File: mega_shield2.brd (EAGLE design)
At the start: 103.8 x 58.7 mm, 36 parts, among them IC1 L298, IC2 LM2937ET-5V, J2 Mega R3

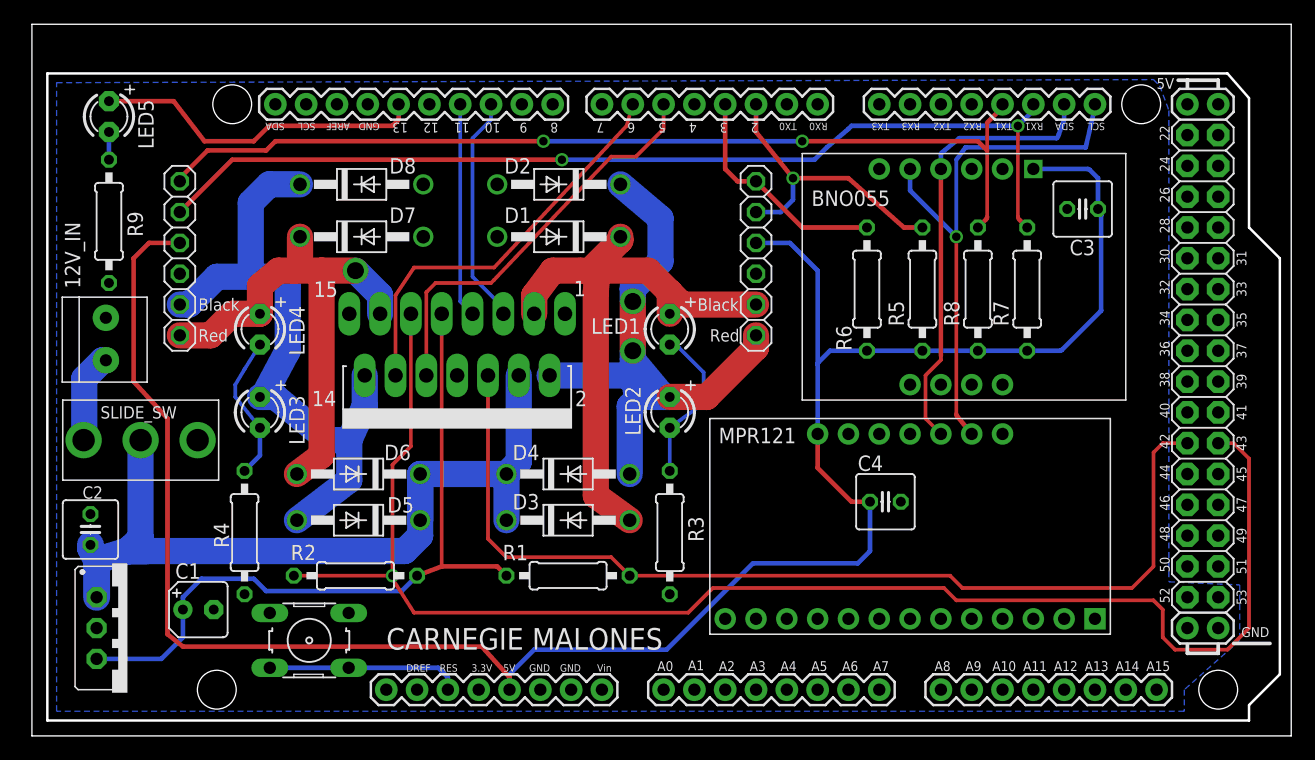
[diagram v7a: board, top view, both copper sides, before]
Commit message: shifted some components around, edited silkscreen
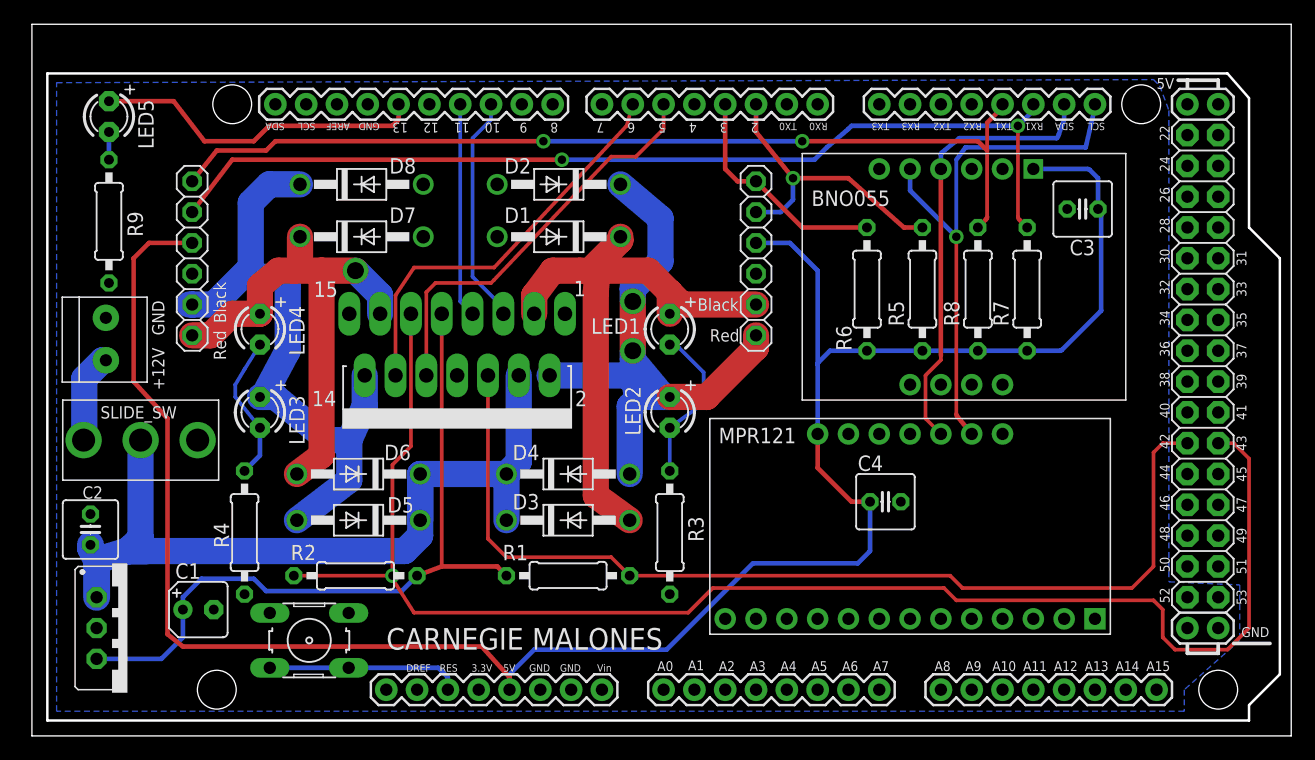
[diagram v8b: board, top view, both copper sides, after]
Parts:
- moved JP2 1.02 mm to (13.2, 39.4)
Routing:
- net MEGA18: track 79.7 -> 78.4 mm
- net MOT3: track 43.1 -> 42.1 mm
- net MEGA_5V: track 176.6 -> 177.6 mm
- net MEGA19: track 83.0 -> 82.3 mm
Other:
- board text added: "+12V"
- board text added: "GND"
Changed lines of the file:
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@@
 <text x="29.21" y="7.112" size="1.778" layer="25">CARNEGIE MALONES</text>
 <polygon width="0.3048" layer="42">
-<vertex x="58.42" y="32.512"/>
+<vertex x="58.674" y="32.004"/>
 <vertex x="58.42" y="32.004"/>
 <vertex x="56.134" y="29.718"/>
 <vertex x="56.134" y="27.432"/>
 <vertex x="56.388" y="27.178"/>
-<vertex x="60.452" y="31.242"/>
-<vertex x="59.69" y="31.242"/>
+<vertex x="59.944" y="30.734"/>
 </polygon>
 <polygon width="0.3048" layer="42">
@@
 <vertex x="33.528" y="16.002"/>
 <vertex x="32.004" y="14.478"/>
-<vertex x="32.004" y="14.224"/>
-<vertex x="32.766" y="13.462"/>
+<vertex x="33.02" y="13.462"/>
 <vertex x="35.306" y="13.462"/>
 <vertex x="38.354" y="16.51"/>
@@
 <vertex x="37.592" y="19.812"/>
 <vertex x="37.338" y="20.066"/>
-</polygon>
-<polygon width="0.4064" layer="42">
-<vertex x="13.716" y="34.29"/>
-<vertex x="13.208" y="34.29"/>
-<vertex x="13.97" y="33.274"/>
-<vertex x="13.97" y="32.512"/>
-<vertex x="13.462" y="32.004"/>
-<vertex x="15.24" y="32.004"/>
-<vertex x="16.764" y="33.528"/>
-<vertex x="16.764" y="33.782"/>
-<vertex x="16.256" y="34.29"/>
-<vertex x="16.256" y="36.322"/>
-<vertex x="15.748" y="36.322"/>
 </polygon>
 <polygon width="0.4064" layer="42">
@@
 <vertex x="72.898" y="32.766"/>
 <vertex x="72.39" y="32.258"/>
-<vertex x="69.596" y="32.258"/>
-<vertex x="69.088" y="32.766"/>
+<vertex x="70.104" y="32.258"/>
+<vertex x="69.342" y="32.766"/>
 <vertex x="68.326" y="32.766"/>
 <vertex x="67.818" y="32.258"/>
@@
 <wire x1="18.542" y1="53.848" x2="18.542" y2="50.8" width="0.4064" layer="42"/>
 <wire x1="18.542" y1="50.8" x2="17.272" y2="48.514" width="0.4064" layer="42"/>
-<wire x1="17.272" y1="48.514" x2="14.478" y2="43.434" width="0.4064" layer="42"/>
-<wire x1="14.478" y1="43.434" x2="13.716" y2="41.91" width="0.4064" layer="42"/>
+<wire x1="17.272" y1="48.514" x2="14.224" y2="42.164" width="0.4064" layer="42"/>
 <wire x1="13.716" y1="41.91" x2="7.874" y2="41.91" width="0.4064" layer="42"/>
 <wire x1="7.874" y1="41.91" x2="2.54" y2="36.576" width="0.4064" layer="42"/>
@@
 <vertex x="15.24" y="31.496"/>
 </polygon>
-<text x="13.716" y="32.512" size="1.016" layer="25">Red</text>
+<text x="16.002" y="30.988" size="1.016" layer="25" rot="R90">Red</text>
 <text x="55.88" y="32.512" size="1.016" layer="25">Red</text>
 <text x="54.864" y="35.052" size="1.016" layer="25">Black</text>
-<text x="13.716" y="35.052" size="1.016" layer="25">Black</text>
+<text x="16.002" y="34.036" size="1.016" layer="25" rot="R90">Black</text>
+<text x="10.922" y="33.02" size="1.016" layer="25" rot="R90">GND</text>
+<text x="9.906" y="32.004" size="1.016" layer="25" rot="R270">+12V</text>
 </plain>
 <attributes>
@@
 </class>
 </classes>
-<designrules name="default">
-<description language="de">&lt;b&gt;EAGLE Design Rules&lt;/b&gt;
-&lt;p&gt;
-Die Standard-Design-Rules sind so gewählt, dass sie für
-die meisten Anwendungen passen. Sollte ihre Platine
-besondere Anforderungen haben, treffen Sie die erforderlichen
-Einstellungen hier und speichern die Design Rules unter
-einem neuen Namen ab.</description>
+<designrules name="SparkFun">
 <description language="en">&lt;b&gt;EAGLE Design Rules&lt;/b&gt;
 &lt;p&gt;
@@
 <param name="mdViaViaSameLayer" value="8mil"/>
 <param name="mnLayersViaInSmd" value="2"/>
-<param name="mdCopperDimension" value="40mil"/>
+<param name="mdCopperDimension" value="10mil"/>
 <param name="mdDrill" value="8mil"/>
 <param name="mdSmdStop" value="0mil"/>
-<param name="msWidth" value="10mil"/>
-<param name="msDrill" value="24mil"/>
+<param name="msWidth" value="8mil"/>
+<param name="msDrill" value="20mil"/>
 <param name="msMicroVia" value="9.99mm"/>
 <param name="msBlindViaRatio" value="0.5"/>
@@
 <param name="rvMicroViaOuter" value="0.25"/>
 <param name="rvMicroViaInner" value="0.25"/>
-<param name="rlMinPadTop" value="10mil"/>
+<param name="rlMinPadTop" value="12mil"/>
 <param name="rlMaxPadTop" value="20mil"/>
 <param name="rlMinPadInner" value="10mil"/>
 <param name="rlMaxPadInner" value="20mil"/>
-<param name="rlMinPadBottom" value="10mil"/>
+<param name="rlMinPadBottom" value="12mil"/>
 <param name="rlMaxPadBottom" value="20mil"/>
-<param name="rlMinViaOuter" value="8mil"/>
+<param name="rlMinViaOuter" value="10mil"/>
 <param name="rlMaxViaOuter" value="20mil"/>
-<param name="rlMinViaInner" value="8mil"/>
+<param name="rlMinViaInner" value="10mil"/>
 <param name="rlMaxViaInner" value="20mil"/>
 <param name="rlMinMicroViaOuter" value="4mil"/>
@@
 <param name="mlMinCreamFrame" value="0mil"/>
 <param name="mlMaxCreamFrame" value="0mil"/>
-<param name="mlViaStopLimit" value="0mil"/>
+<param name="mlViaStopLimit" value="25mil"/>
 <param name="srRoundness" value="0"/>
 <param name="srMinRoundness" value="0mil"/>
@@
 </autorouter>
 <elements>
-<element name="12V_IN" library="adafruit" package="1X2-3.5MM" value="1X2-3.5MM" x="6.096" y="32.766" smashed="yes" rot="R270">
-<attribute name="NAME" x="3.984" y="36.878" size="1.27" layer="25" rot="R90"/>
-</element>
+<element name="12V_IN" library="adafruit" package="1X2-3.5MM" value="1X2-3.5MM" x="6.096" y="32.766" smashed="yes" rot="R270"/>
 <element name="C1" library="rcl" package="B45181A" value="22 uF" x="13.716" y="10.414" smashed="yes">
 <attribute name="NAME" x="11.811" y="12.954" size="1.27" layer="25" ratio="10"/>
@@
 <attribute name="VALUE" x="57.785" y="38.862" size="1.27" layer="27" rot="R90"/>
 </element>
-<element name="JP2" library="adafruit" package="1X06" value="MOTOR_2" x="12.192" y="39.37" smashed="yes" rot="R90">
-<attribute name="VALUE" x="15.367" y="39.116" size="1.27" layer="27" rot="R90"/>
+<element name="JP2" library="adafruit" package="1X06" value="MOTOR_2" x="13.208" y="39.37" smashed="yes" rot="R90">
+<attribute name="VALUE" x="16.383" y="39.116" size="1.27" layer="27" rot="R90"/>
 </element>
 <element name="SLIDE_SW" library="arduinoShield" package="E-SWITCH_500SSP1S2M2QEA" value="E-SWITCH_500SSP1S2M2QEA" x="6.35" y="23.622" smashed="yes" rot="R90">
@@
 <wire x1="81.35439375" y1="42.59760625" x2="82.042" y2="41.91" width="0.381" layer="1"/>
 <contactref element="JP2" pad="5"/>
-<wire x1="12.192" y1="43.18" x2="16.51" y2="47.498" width="0.381" layer="1"/>
+<wire x1="13.208" y1="43.18" x2="16.51" y2="47.498" width="0.381" layer="1"/>
 <wire x1="65.532" y1="48.514" x2="67.31" y2="50.038" width="0.381" layer="16"/>
 <wire x1="82.47560625" y1="51.48760625" x2="81.28" y2="50.292" width="0.381" layer="16"/>
@@
 <wire x1="78.66560625" y1="42.59760625" x2="77.978" y2="41.91" width="0.381" layer="1"/>
 <contactref element="JP2" pad="6"/>
-<wire x1="12.192" y1="45.72" x2="11.938" y2="45.72" width="0.381" layer="1"/>
-<wire x1="11.938" y1="45.72" x2="14.478" y2="48.26" width="0.381" layer="1"/>
-<wire x1="14.478" y1="48.26" x2="19.304" y2="48.26" width="0.381" layer="1"/>
+<wire x1="13.208" y1="45.72" x2="15.24" y2="48.26" width="0.381" layer="1"/>
+<wire x1="15.24" y1="48.26" x2="19.304" y2="48.26" width="0.381" layer="1"/>
 <wire x1="19.304" y1="48.26" x2="20.066" y2="49.022" width="0.381" layer="1"/>
 <wire x1="20.066" y1="49.022" x2="42.164" y2="49.022" width="0.381" layer="1"/>
@@
 <wire x1="62.484" y1="40.64" x2="64.77" y2="38.354" width="0.381" layer="16"/>
 <wire x1="64.77" y1="38.354" x2="64.77" y2="30.628790625" width="0.381" layer="16"/>
-<wire x1="12.192" y1="40.64" x2="9.652" y2="40.64" width="0.381" layer="1"/>
+<wire x1="13.208" y1="40.64" x2="9.652" y2="40.64" width="0.381" layer="1"/>
 <wire x1="9.652" y1="40.64" x2="8.382" y2="39.37" width="0.381" layer="1"/>
 <wire x1="12.446" y1="7.366" x2="37.084" y2="7.366" width="0.381" layer="1"/>
@@
 <wire x1="18.796" y1="34.798" x2="16.51" y2="34.798" width="2.159" layer="1"/>
 <wire x1="16.51" y1="34.798" x2="14.732" y2="33.02" width="2.159" layer="1"/>
-<wire x1="14.732" y1="33.02" x2="12.192" y2="33.02" width="2.159" layer="1"/>
+<wire x1="14.732" y1="33.02" x2="13.208" y2="33.02" width="2.159" layer="1"/>
 <wire x1="18.796" y1="34.798" x2="18.796" y2="37.084" width="2.159" layer="1"/>
 <wire x1="18.796" y1="37.084" x2="20.32" y2="38.354" width="2.159" layer="1"/>
@@
 <wire x1="27.432" y1="27.178" x2="26.162" y2="24.384" width="2.159" layer="16"/>
 <contactref element="JP2" pad="2"/>
-<wire x1="12.192" y1="35.56" x2="12.954" y2="35.56" width="2.159" layer="16"/>
-<wire x1="12.954" y1="35.56" x2="15.24" y2="37.846" width="2.159" layer="16"/>
-<wire x1="15.24" y1="37.846" x2="18.034" y2="37.846" width="2.159" layer="16"/>
+<wire x1="13.208" y1="35.56" x2="12.954" y2="35.56" width="2.159" layer="16"/>
 <wire x1="18.034" y1="37.846" x2="20.574" y2="37.846" width="2.159" layer="16"/>
 <wire x1="20.574" y1="37.846" x2="20.701" y2="37.719" width="2.159" layer="16"/>
 <wire x1="22.098" y1="45.466" x2="19.558" y2="45.466" width="2.159" layer="16"/>
 <wire x1="19.558" y1="45.466" x2="18.034" y2="43.942" width="2.159" layer="16"/>
-<wire x1="18.034" y1="43.942" x2="18.034" y2="37.846" width="2.159" layer="16"/>
+<wire x1="18.034" y1="43.942" x2="18.034" y2="38.608" width="2.159" layer="16"/>
+<wire x1="18.034" y1="38.608" x2="18.034" y2="37.846" width="2.159" layer="16"/>
 <wire x1="21.082" y1="37.084" x2="21.082" y2="31.75" width="2.159" layer="16"/>
-</signal>
-<signal name="+12V">
+<wire x1="13.208" y1="35.56" x2="14.986" y2="35.56" width="2.159" layer="16"/>
+<wire x1="14.986" y1="35.56" x2="18.034" y2="38.608" width="2.159" layer="16"/>
+</signal>
+<signal name="+12V" class="1">
 <contactref element="12V_IN" pad="1"/>
 <contactref element="SLIDE_SW" pad="L1"/>
